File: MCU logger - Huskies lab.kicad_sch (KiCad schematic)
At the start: 25 parts, among them U1 ATMEGA328P-AU, U2 DS1337S+, U3 24LC1025, U4 24LC1025, Y1 32.768KHz, Y2 16Mhz

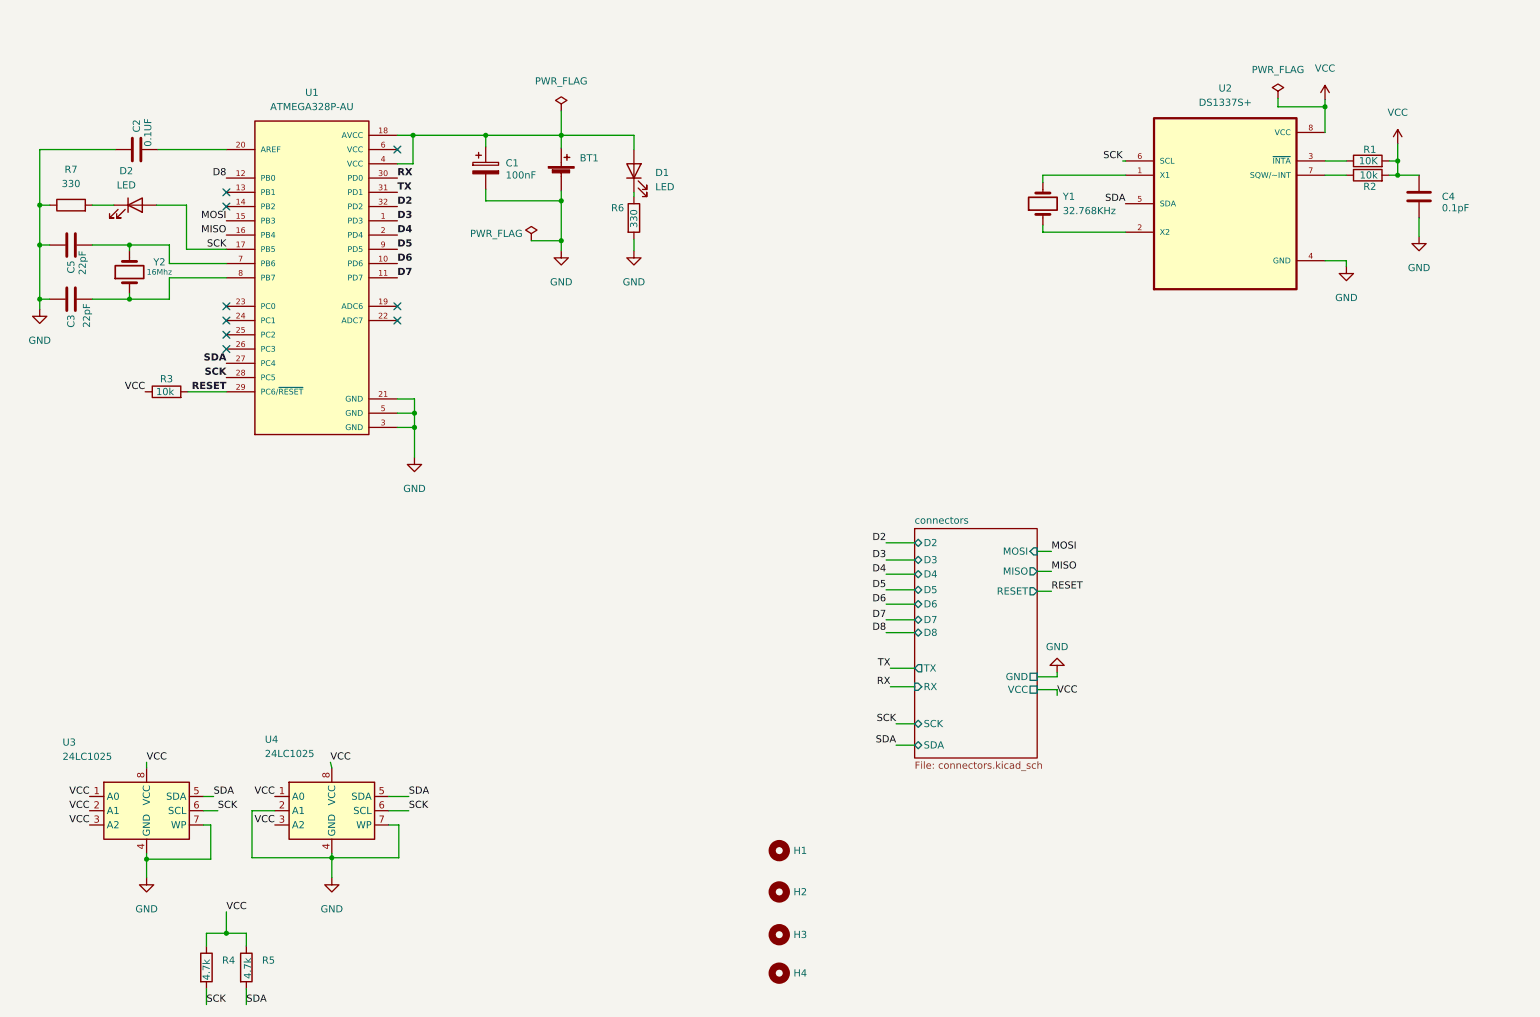
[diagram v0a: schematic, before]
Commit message: senalizacion del esquematico.
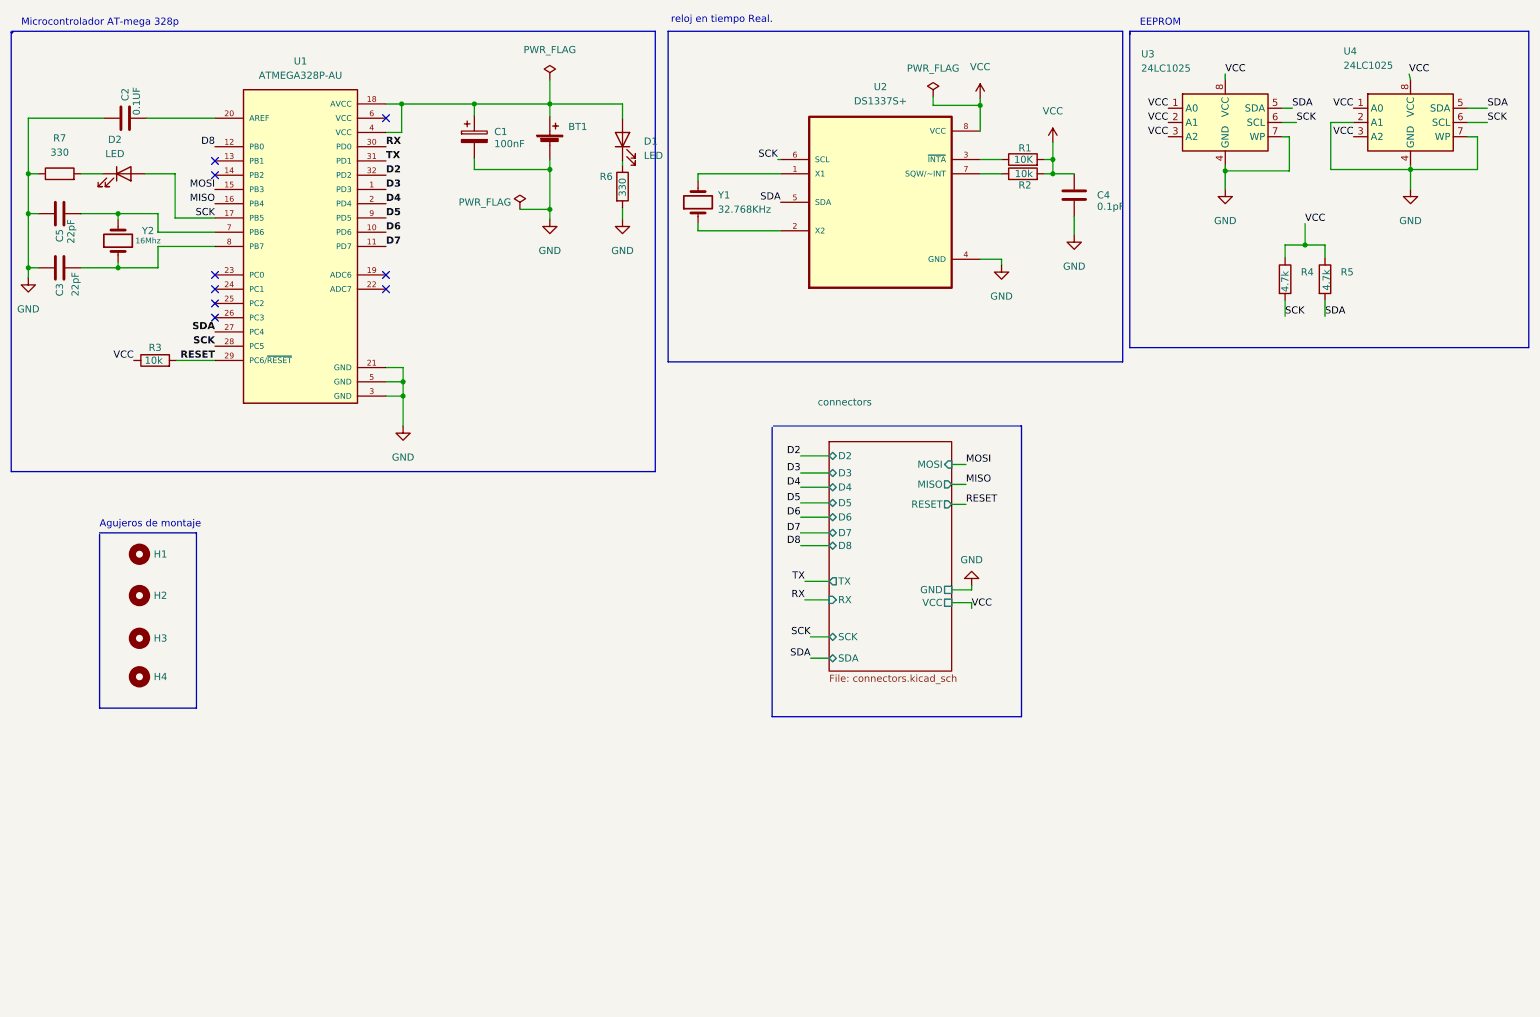
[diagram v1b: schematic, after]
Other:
- note added: "Agujeros de montaje"
- note added: "EEPROM"
- note added: "Microcontrolador AT-mega 328p"
- note added: "reloj en tiempo Real."
- moved on the sheet: BT1, C1, C2, C3, C4, C5, D1, D2, H1, H2, H3, H4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
